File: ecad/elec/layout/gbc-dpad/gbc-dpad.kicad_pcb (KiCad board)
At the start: 2 copper layers, 9 parts

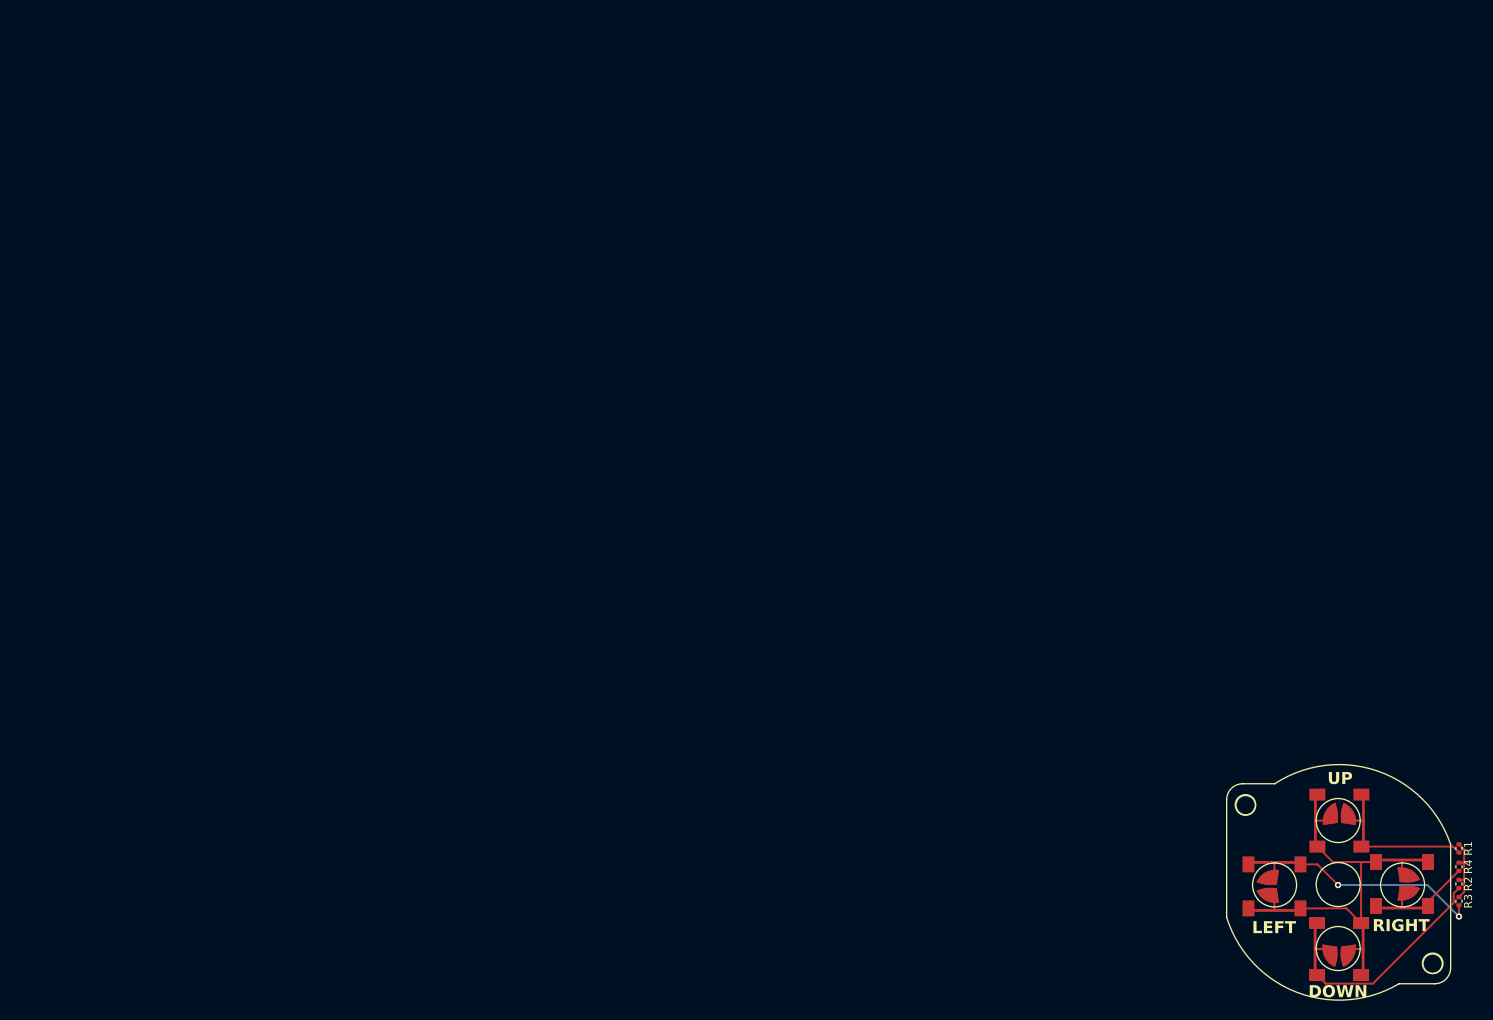
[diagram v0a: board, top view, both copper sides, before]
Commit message: feat(ecad): Update ECAD to support latest atopile and fix some bugs (#119)
* feat(ecad): Update ecad / atopile and improve workflow

* add step file to repo

* add box-3 step file

* improve workflow

* update the action to latest and fix some bugs / spurious issues

* remove legacy files

* update readme

* update deprecations

* improve placement of components and robustness of scripts

* nudge layouts some

* further layout changes

* fixing some issues

* fix broken ci

* minor update

* simple layout

* update to work with latest atopile services (lack thereof)

* update routing

* fix(ecad): vendor atopile registry package for CI builds

packages.atopileapi.com no longer resolves (taken down in the 0.16
platform migration, like the components API), so dependency resolution
of atopile/ti-tps63020@0.4.0 fails in CI and on any machine without a
warm .ato/modules. Commit the installed package (sans .cache) so
`ato build` finds it via its installed-package path and never contacts
the dead registry.

Co-Authored-By: Claude Fable 5 <noreply@anthropic.com>

* fix(ecad): keep vendored package byte-exact (no EOL normalization)

ato validates installed packages against the file hashes in
.package_meta.json; git's CRLF->LF normalization of the STEP files
changed their bytes on checkout, making CI fail with "Package has
local modifications". Exempt ecad/.ato/modules from text normalization
and re-commit the original bytes.

Co-Authored-By: Claude Fable 5 <noreply@anthropic.com>

* fix(ci): disable baked-in ATO_FROZEN and normalize base layout serialization

The atopile-kicad docker image sets ATO_FROZEN=1, silently forcing CI
builds into frozen mode, which fails on phantom in-memory diffs
(locked-attribute defaults, arc direction normalization) that never
reach the file on disk. Pass ATO_FROZEN=0 from the workflow — we verify
layout stability ourselves via canonicalize + git diff.

Also re-serialize box-emu-base.kicad_pcb through the same container
build + canonicalize pip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
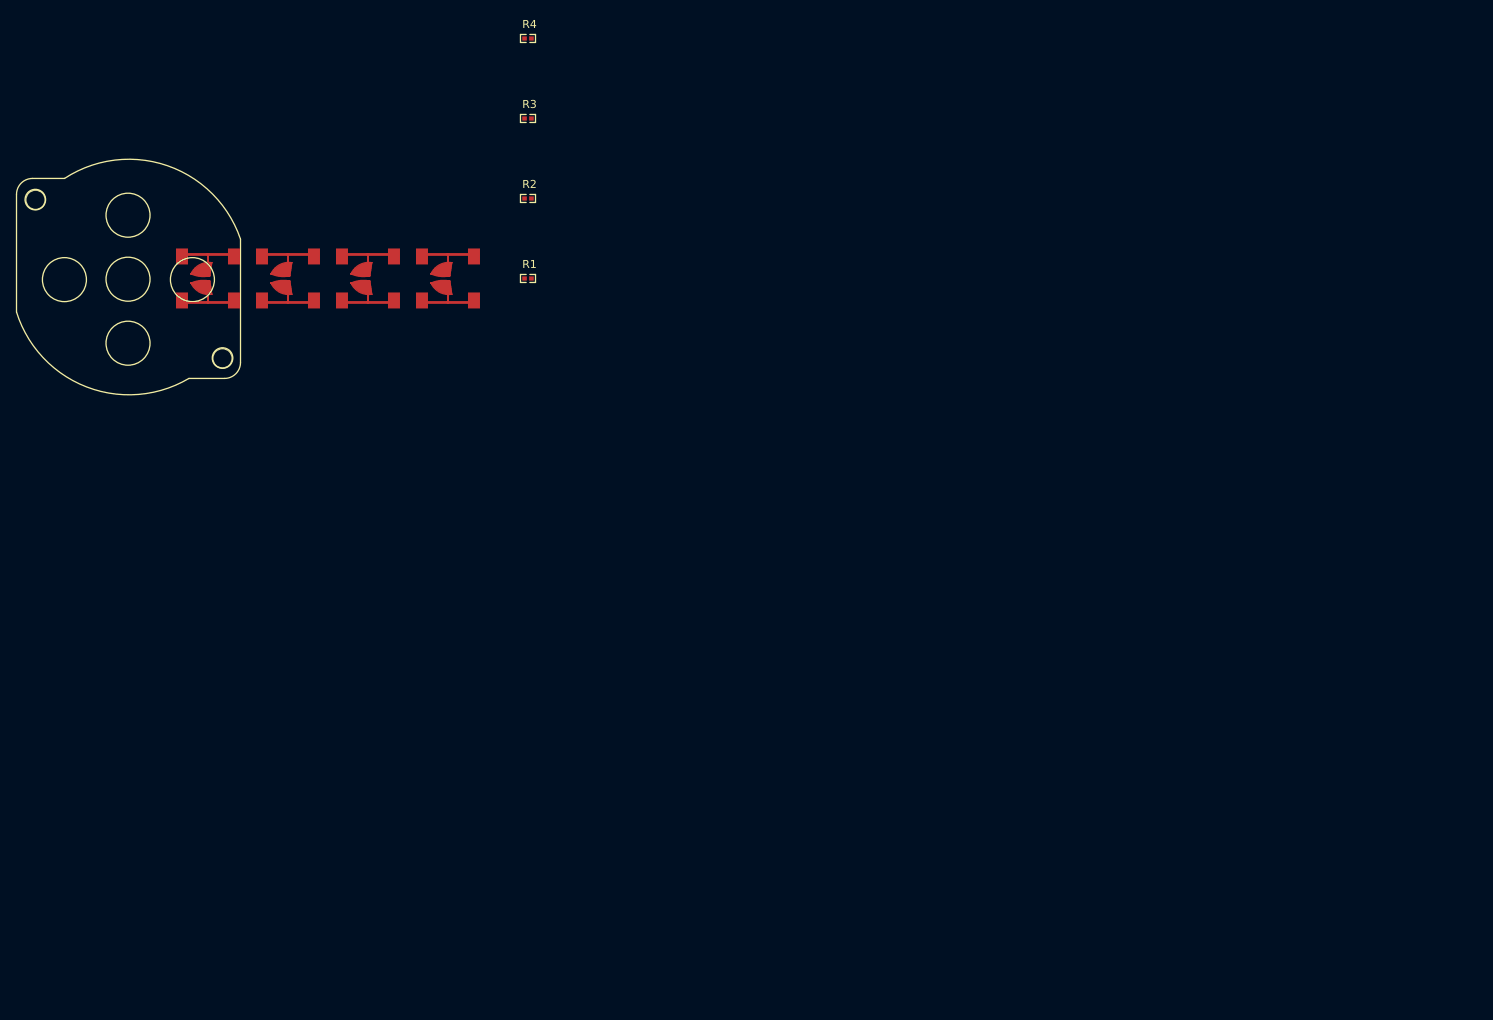
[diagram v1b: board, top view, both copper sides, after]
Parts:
- removed U1: , lib:GAMEBOY_COLOR_DPAD_MEMBRANE
- removed U2, U3, U4, U5: , lib:GBC_DPAD_BUTTON
- added MECH1: , GBC_DPAD_MEMBRANE:GAMEBOY_COLOR_DPAD_MEMBRANE, F.Cu at (0.00, 0.00)
- added SW1: , GBC_DPAD_BUTTON:GBC_DPAD_BUTTON, F.Cu at (20.0, 0.00)
- added SW2: , GBC_DPAD_BUTTON:GBC_DPAD_BUTTON, F.Cu at (30.0, 0.00)
- added SW3: , GBC_DPAD_BUTTON:GBC_DPAD_BUTTON, F.Cu at (40.0, 0.00)
- added SW4: , GBC_DPAD_BUTTON:GBC_DPAD_BUTTON, F.Cu at (10.0, 0.00)
- R1, R2, R3, R4: value 62.5mW Thick Film Resistors 50V ±100ppm/℃ ±1% 10kΩ 0402 Chip Resistor - Surface Mount ROHS -> 10kΩ ±5%; footprint lib:R0402 -> UNI_ROYAL_0402WGF1002TCE:R0402
- moved R4 155.8 mm to (50.0, -30.0), turned to 0 degrees
- moved R3 152.0 mm to (50.0, -20.0), turned to 0 degrees
- moved R2 144.5 mm to (50.0, -10.0), turned to 0 degrees
- moved R1 136.4 mm to (50.0, 0.00), turned to 0 degrees
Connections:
- net vcc renamed hv
- R1 pad 2: up -> contact_in
- R2 pad 2: down -> left_button-out-contact_in
- R3 pad 2: left -> right_button-out-contact_in
- R4 pad 2: right -> up_button-out-contact_in
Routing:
- net gnd: track 51.0 -> 0.00 mm
- net left: track 30.6 -> 0.00 mm, vias 2 -> 0
- net down: track 30.5 -> 0.00 mm
- net up: track 19.2 -> 0.00 mm
- net right: track 12.7 -> 0.00 mm
- net hv: track 8.53 -> 0.00 mm
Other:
- board text removed: "DOWN"
- board text removed: "LEFT"
- board text removed: "RIGHT"
- board text removed: "UP"
